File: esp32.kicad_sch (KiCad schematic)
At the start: 25 parts, among them J12 DAT0, J13 DAT_DSP_1..8, J14 + -, J15 DAT_DSP_9..14, Q18 2N3904, Q19 2N3904, Q20 2N3904, U10 74LS241, U11 74LS241, U12 74LS241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

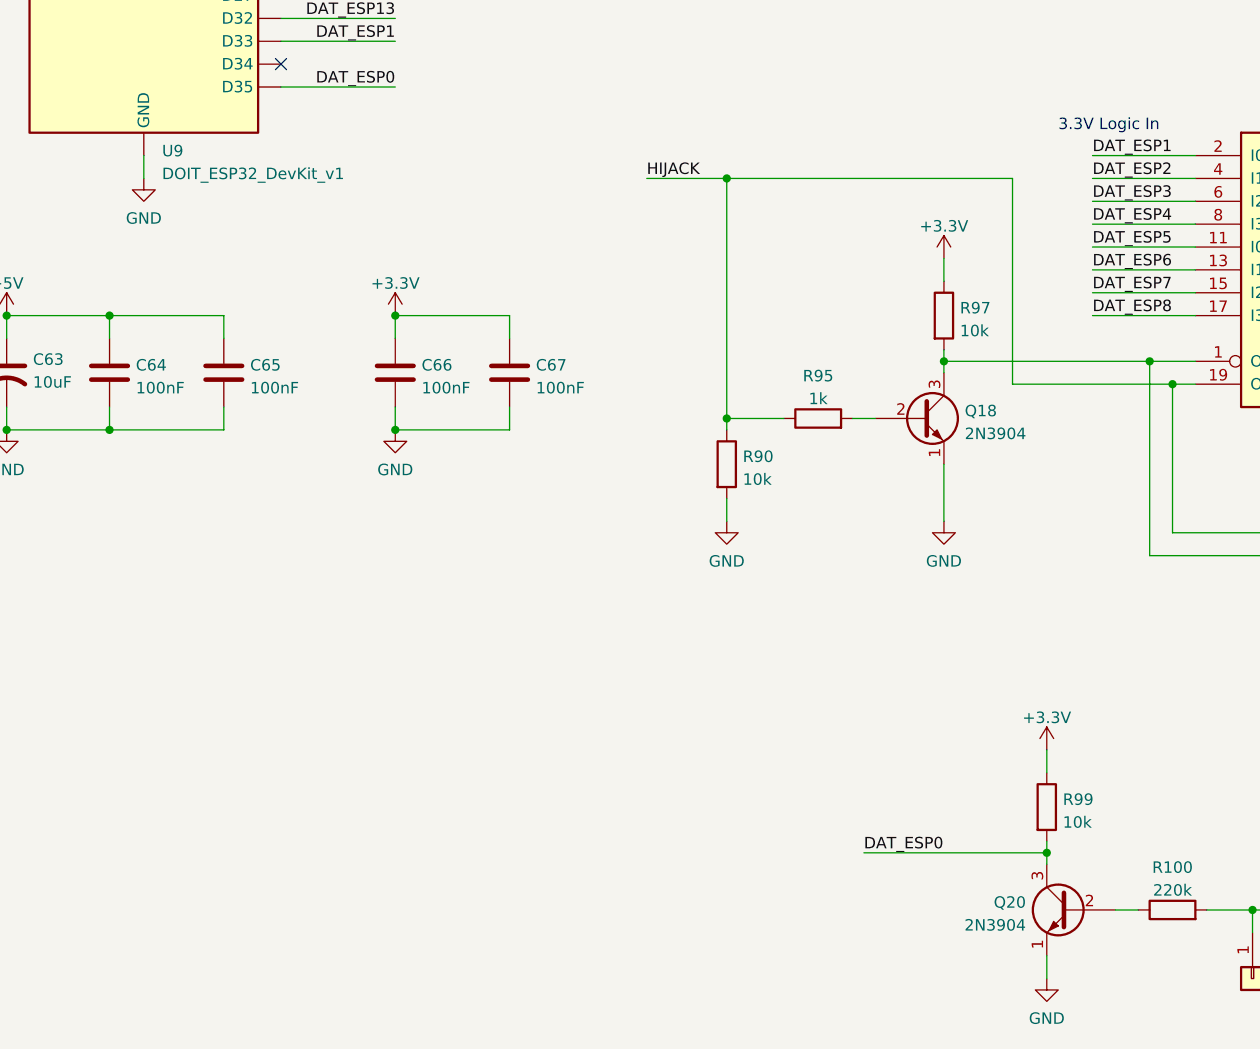
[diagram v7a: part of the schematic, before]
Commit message: added bom exclusions for non mod components
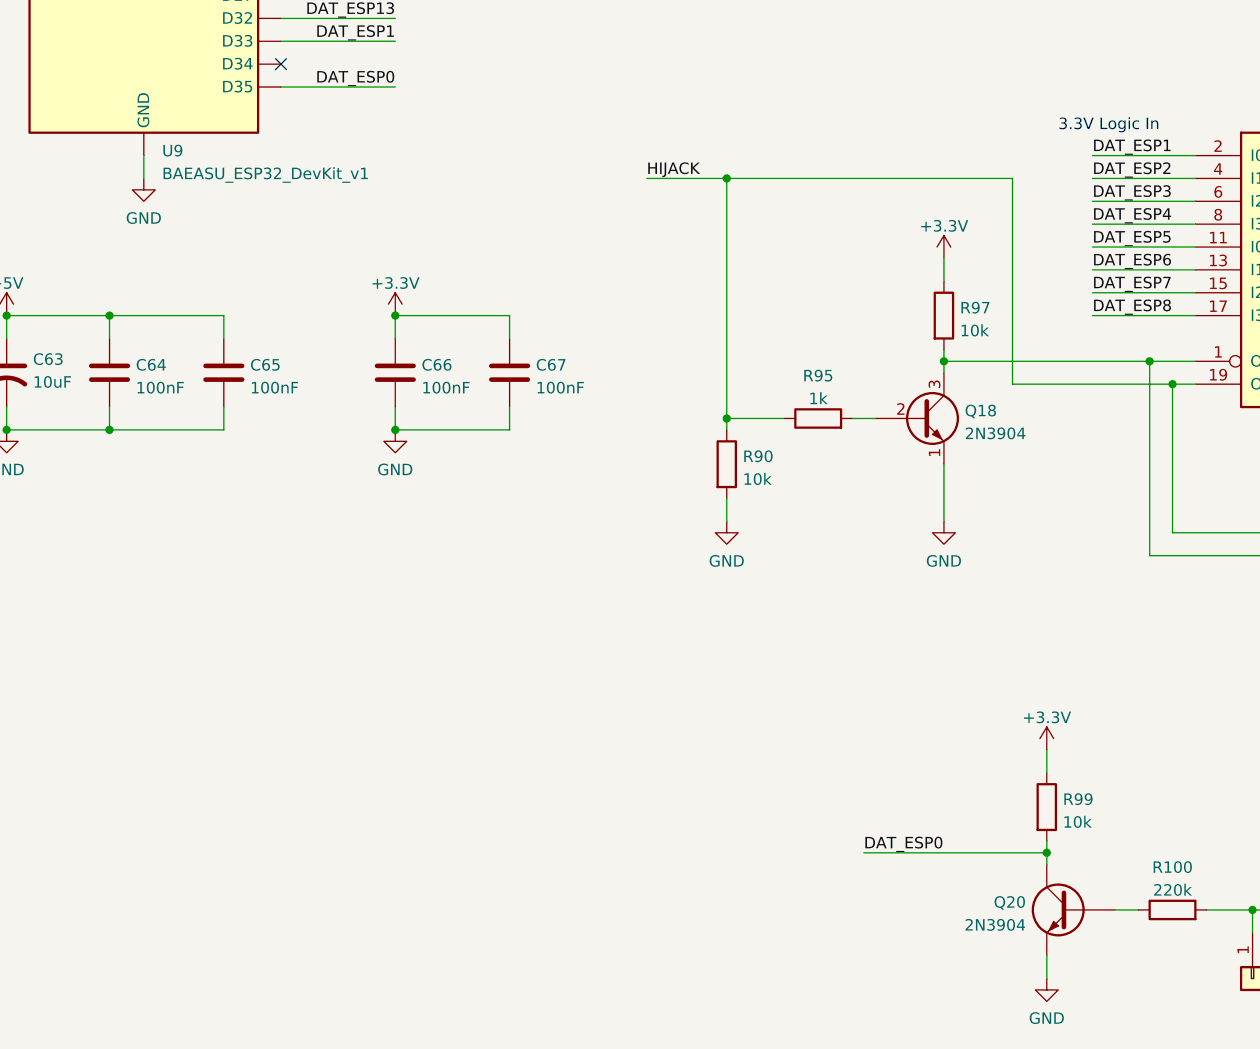
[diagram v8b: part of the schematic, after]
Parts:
- Q20: footprint Package_TO_SOT_THT:TO-92_Inline -> Package_TO_SOT_THT:TO-92_Inline_Wide
- U9: value DOIT_ESP32_DevKit_v1 -> BAEASU_ESP32_DevKit_v1
